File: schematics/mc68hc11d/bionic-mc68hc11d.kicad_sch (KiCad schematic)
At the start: 8 parts, among them J1 Bionic-P135, J2 Bionic-P245, U1 MC68HC11D0P, U2 11AA010-I/TT

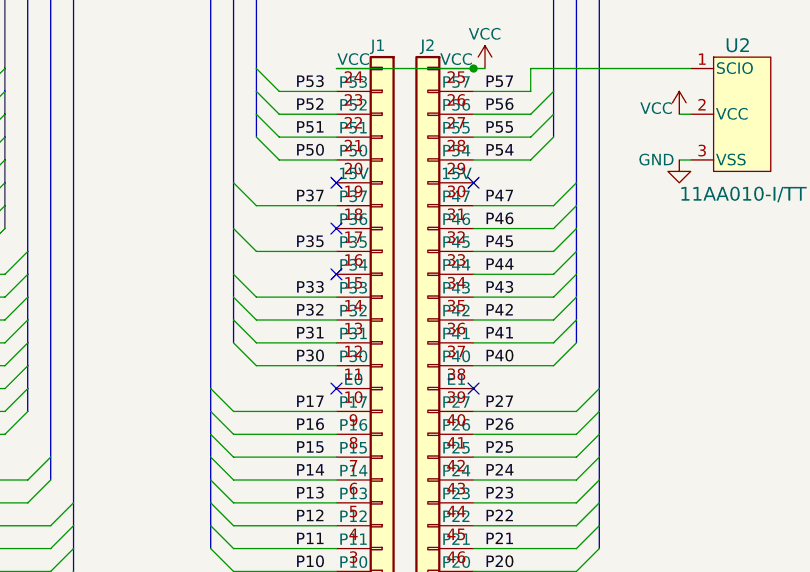
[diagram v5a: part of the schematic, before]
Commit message: [MC68HC11D] Update schematics
Remove unused pins from bionic connector
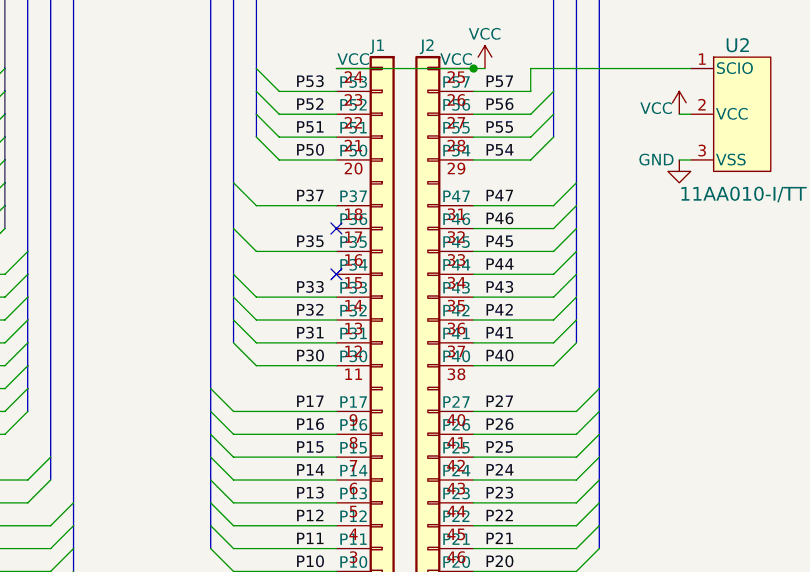
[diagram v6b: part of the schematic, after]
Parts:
- J1: footprint bionic:Bionic-P135_Vertical -> bionic:Bionic-P135_THT
- J2: footprint bionic:Bionic-P245_Vertical -> bionic:Bionic-P245_THT
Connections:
- no-connect marks 7 -> 3
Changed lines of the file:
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@@
 	(title_block
 		(title "BionicMC68HC11D")
-		(date "2024-11-01")
-		(rev "8")
+		(date "2025-03-02")
+		(rev "9")
 		(company "Tadashi G. Takaoka")
 	)
@@
 	)
 	(no_connect
-		(at 143.51 115.57)
-	)
-	(no_connect
 		(at 143.51 102.87)
 	)
 	(no_connect
-		(at 158.75 92.71)
-	)
-	(no_connect
-		(at 158.75 115.57)
-	)
-	(no_connect
 		(at 143.51 97.79)
 	)
-	(no_connect
-		(at 143.51 92.71)
-	)
 	(bus_entry
 		(at 63.5 100.33)
@@
 			)
 		)
-		(property "Footprint" "bionic:Bionic-P245_Vertical"
+		(property "Footprint" "bionic:Bionic-P245_THT"
 			(at 158.75 143.51 0)
 			(effects
@@
 		(pin "45"
 		)
-		(pin "39"
-		)
 		(pin "43"
 		)
@@
 		(pin "40"
 		)
-		(pin "30"
-		)
 		(pin "28"
 		)
@@
 			)
 		)
-		(property "Footprint" "bionic:Bionic-P135_Vertical"
+		(property "Footprint" "bionic:Bionic-P135_THT"
 			(at 149.86 143.51 0)
 			(effects
@@
 		(pin "12"
 		)
-		(pin "10"
-		)
 		(pin "11"
 		)
@@
 		(pin "21"
 		)
-		(pin "19"
-		)
 		(pin "18"
